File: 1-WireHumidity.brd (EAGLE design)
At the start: 49.8 x 7.6 mm, 10 parts, among them U1 DS2438Z+, U2 HIH-4030SMD

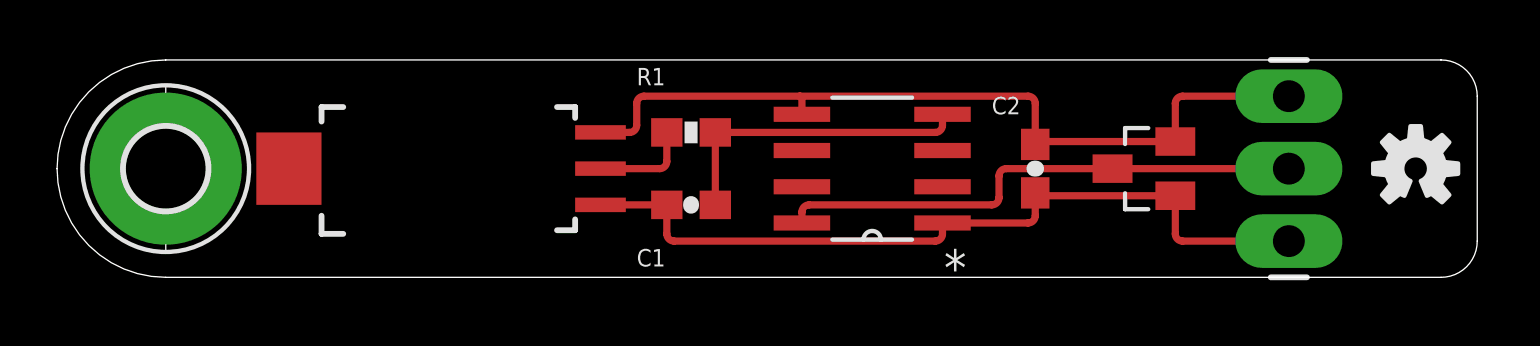
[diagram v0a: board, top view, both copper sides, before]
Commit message: Little board lenght adjustment (now 5cm)
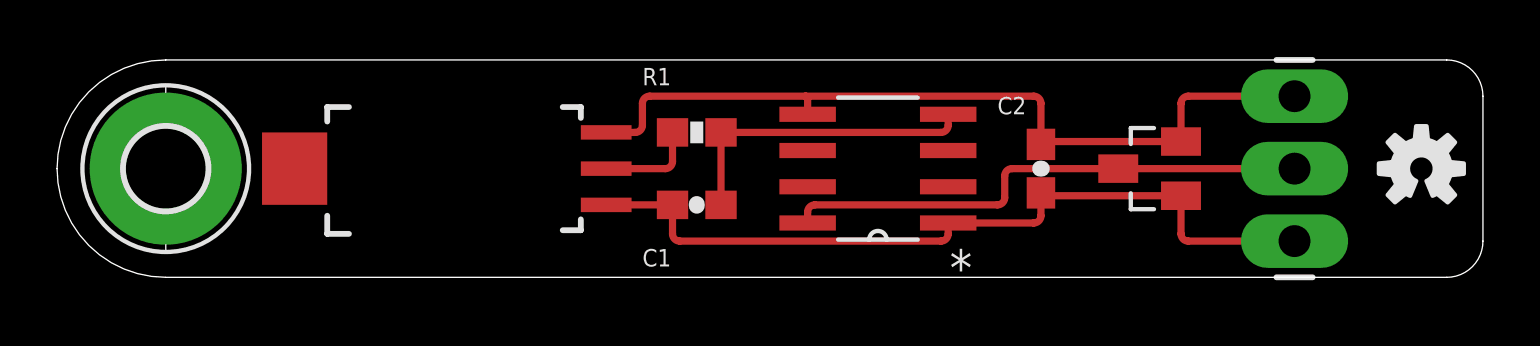
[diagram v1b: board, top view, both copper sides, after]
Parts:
- moved C2 0.20 mm to (34.5, 3.81)
- moved JP2 0.20 mm to (43.4, 6.35)
- moved U$1 0.20 mm to (47.8, 3.81)
- moved C1 0.20 mm to (22.4, 2.54)
- moved R1 0.20 mm to (22.4, 5.08)
- moved U1 0.20 mm to (28.8, 3.81)
- moved U2 0.20 mm to (14.2, 3.81)
- moved D1 0.20 mm to (38.3, 3.81)
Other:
- board size 49.8 x 7.6 mm -> 50 x 7.6 mm
